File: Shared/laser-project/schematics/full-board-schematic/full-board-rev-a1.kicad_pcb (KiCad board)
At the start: 2 copper layers, 116.8 x 53.3 mm, 38 parts, among them CON1 ENCODER-10MIL-HEADER, CON2 JTAG-10MIL-HDR, T1 BSS138, T2 BSS138, T3 OP598C, U1 TEENSYPP2, U2 MCP1825, U3 DS1077, U4 AD8302, U5 MCP1825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

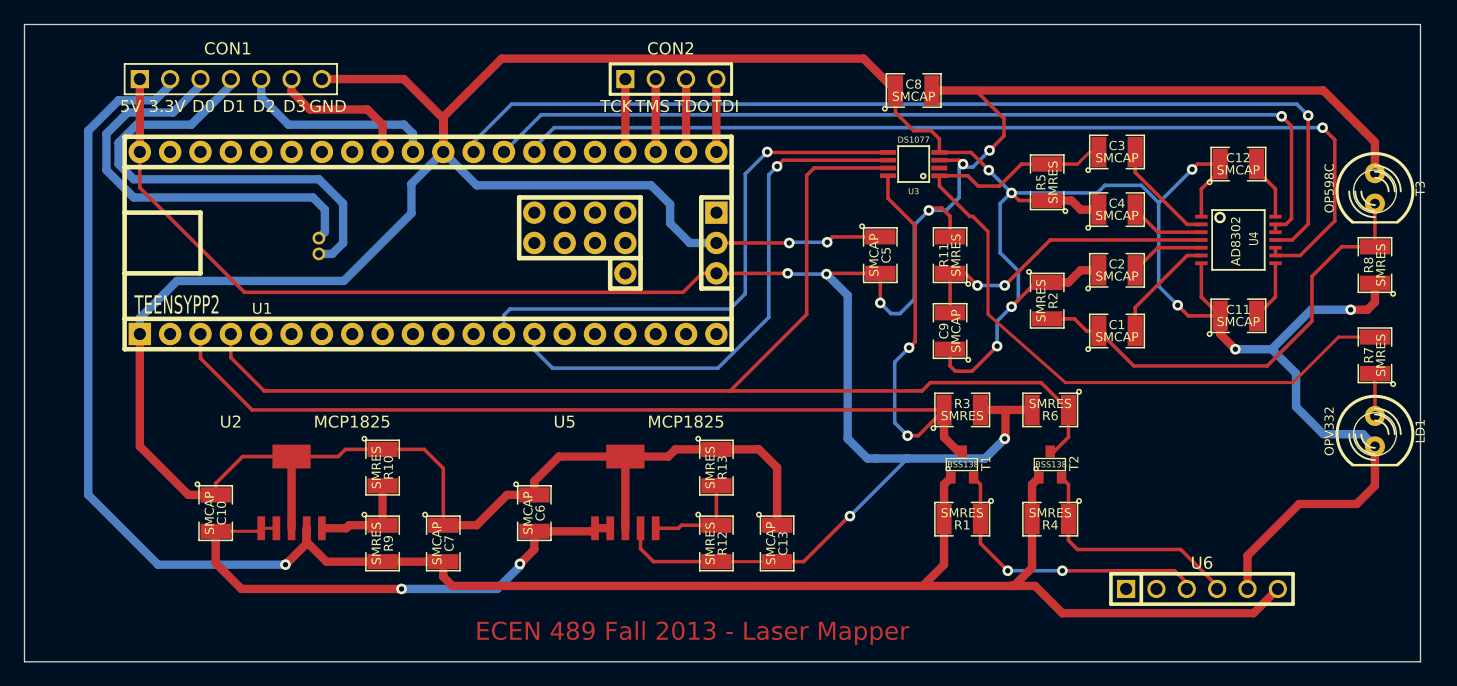
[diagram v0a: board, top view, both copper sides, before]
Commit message: 
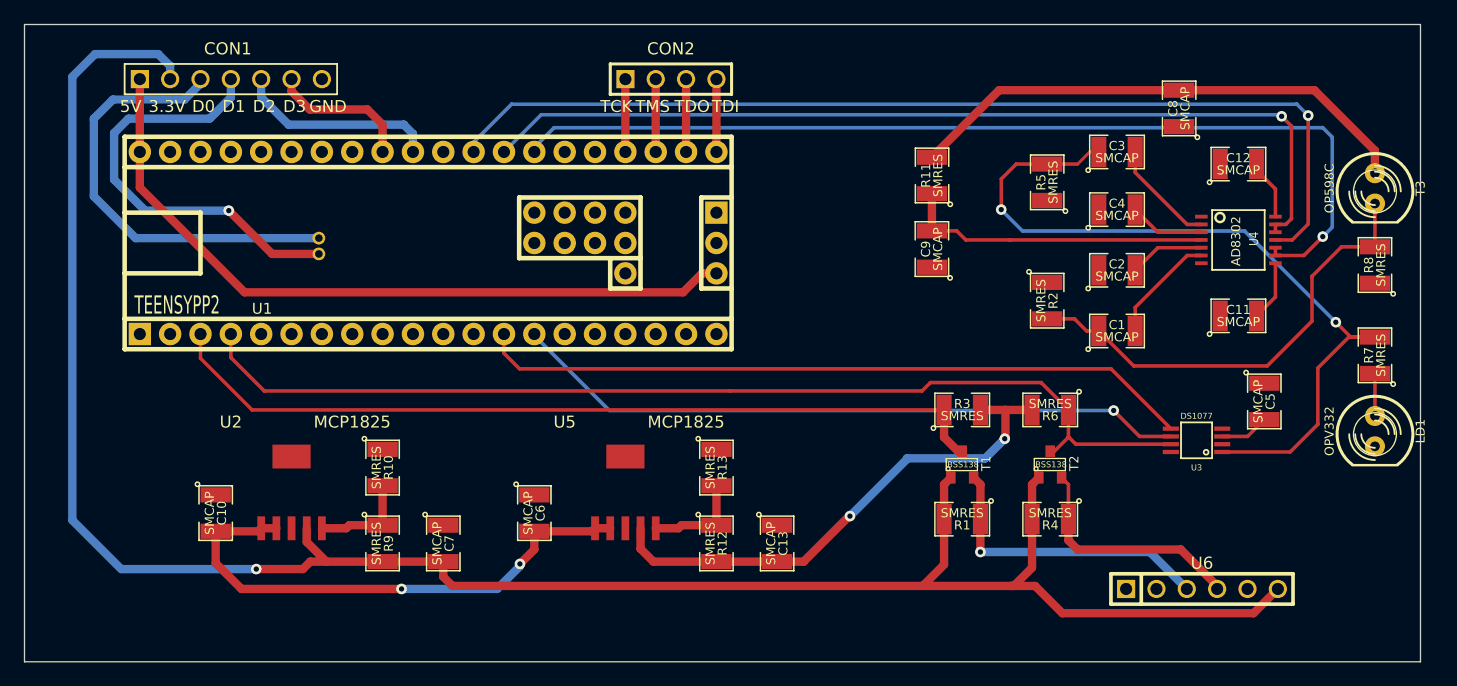
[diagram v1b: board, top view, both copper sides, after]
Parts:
- U3: footprint SO8N -> SO8N_good
- moved C5 34.4 mm to (268.9, 128.1)
- moved U3 33.1 mm to (263.2, 131.3)
- moved C8 22.3 mm to (261.7, 103.5), turned to 90 degrees
- moved C9 7.03 mm to (241.0, 115.3)
- moved R11 6.84 mm to (241.1, 109.2)
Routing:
- net GND: track 372.3 -> 0.00 mm, vias 10 -> 0
- net /regulator_5V: track 220.0 -> 152.9 mm, vias 8 -> 2
- net /twi_scl_5V: track 98.2 -> 70.4 mm, vias 2 -> 0
- net /twi_sda_5V: track 106.5 -> 87.6 mm
- net /osc_ctrl0: track 45.3 -> 60.0 mm, vias 1 -> 0
- net /osc_ctrl1: track 45.8 -> 56.9 mm
- net /regulator_3.3V: track 168.8 -> 177.5 mm
- net /encoder-interface-1: track 39.6 -> 36.2 mm, vias 0 -> 1
- net /mod_sig_1: track 64.4 -> 66.9 mm, vias 0 -> 2
- net /encoder-interface-0: track 35.4 -> 37.3 mm
- net /ad8302_vpos: track 26.3 -> 26.0 mm, vias 2 -> 0
- net /twi_scl_3.3V: track 24.9 -> 25.0 mm, vias 2 -> 1
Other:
- board text removed: "ECEN 489 Fall 2013 - Laser Mapper"

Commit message: Forgot to commit the board file.
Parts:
- moved LD1 8.13 mm to (278.4, 122.4), turned to 90 degrees
- moved R7 3.31 mm to (278.4, 127.5), turned to 180 degrees
- moved T3 2.05 mm to (278.4, 112.3)
- moved R8 0.74 mm to (278.4, 117.3), turned to 180 degrees
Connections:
- C10 pad 2: /usb_5V -> /teensy_5V
- C6 pad 2: /usb_5V -> /teensy_5V
- U1 pad 52: /regulator_5V -> /teensy_5V
- U2 pad 1: /usb_5V -> /teensy_5V
- U2 pad 2: /usb_5V -> /teensy_5V
- U5 pad 1: /usb_5V -> /teensy_5V
- U5 pad 2: /usb_5V -> /teensy_5V
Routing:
- net GND: track 0.00 -> 362.9 mm, vias 0 -> 7
- net /regulator_5V: track 152.9 -> 265.3 mm, vias 2 -> 5
- net /teensy_5V: track 0.00 -> 83.7 mm, vias 0 -> 2
- net /usb_5V: track 44.9 -> 0.00 mm, vias 2 -> 0
- net /twi_scl_5V: track 70.4 -> 88.9 mm, vias 0 -> 2
- net /mod_sig_1: track 66.9 -> 55.6 mm
- net /encoder-interface-1: track 36.2 -> 42.6 mm, vias 1 -> 0
- net /osc_ctrl1: track 56.9 -> 58.0 mm, vias 1 -> 2
- net N-000001: track 3.56 -> 4.44 mm
- net /return_sig: track 39.0 -> 38.3 mm
- net /regulator_3.3V: track 177.5 -> 176.9 mm

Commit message: Addition of the op-amp, ground planes, and milling finalization.
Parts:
- added U7: TI-OPA2356, MSOP_8, F.Cu at (275.3, 132.1)
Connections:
- R7 pad 2: /mod_sig_1 -> /laser_drive_sig
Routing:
- net /regulator_5V: track 265.3 -> 287.9 mm, vias 5 -> 6
- net GND: track 362.9 -> 372.5 mm
- net /laser_drive_sig: track 0.00 -> 8.17 mm
- net /mod_sig_1: track 55.6 -> 54.4 mm
- added copper zone on B.Cu, net GND
- added copper zone on F.Cu, net GND
